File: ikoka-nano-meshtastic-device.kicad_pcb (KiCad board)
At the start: 2 copper layers, 28 x 40 mm, 7 parts, among them J1 Battery, J2 Solar, J3 Qwiic_RA, Q1 Q_PMOS_GSD, U1 Seeed Studio XIAO nRF52840, U2 E22-900M30S

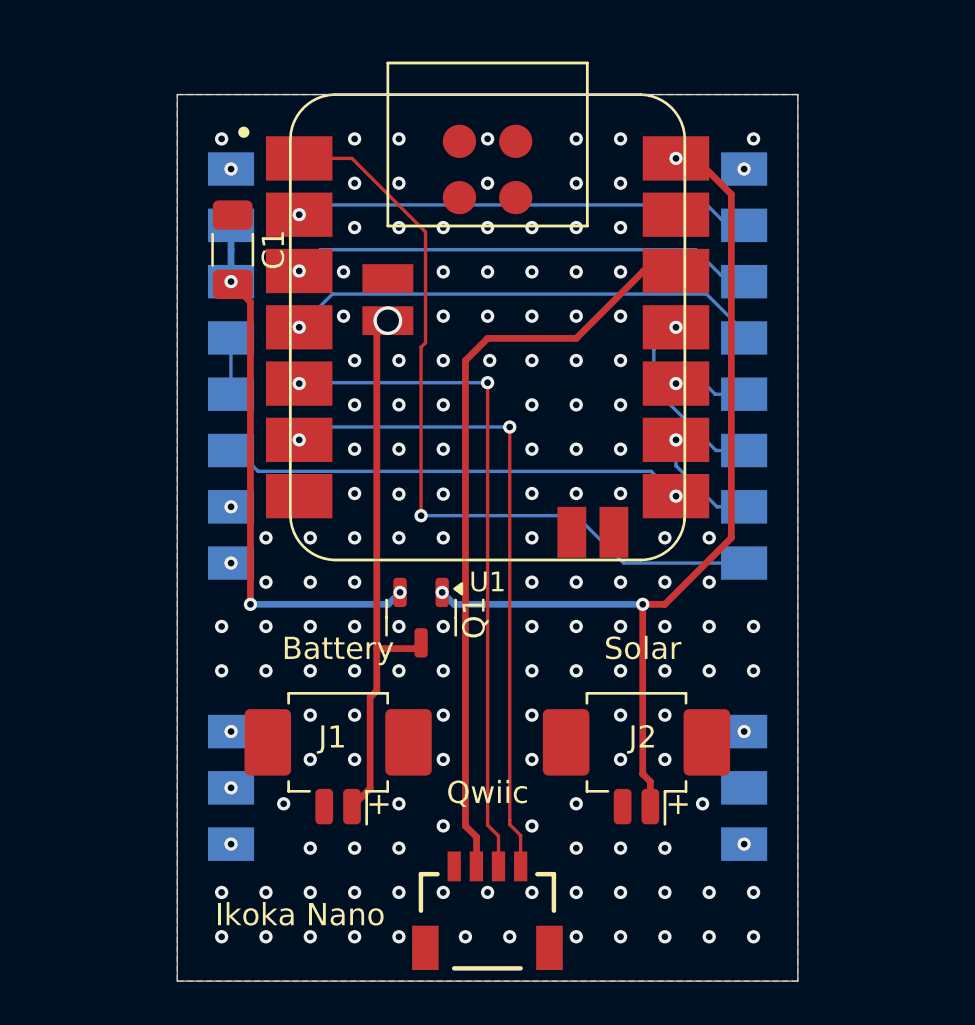
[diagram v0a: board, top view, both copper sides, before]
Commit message: Add missing D1 footprint and update PCB; add LCSC part numbers; remove gerbers
Signed-off-by: Andrew Yong <me@ndoo.sg>
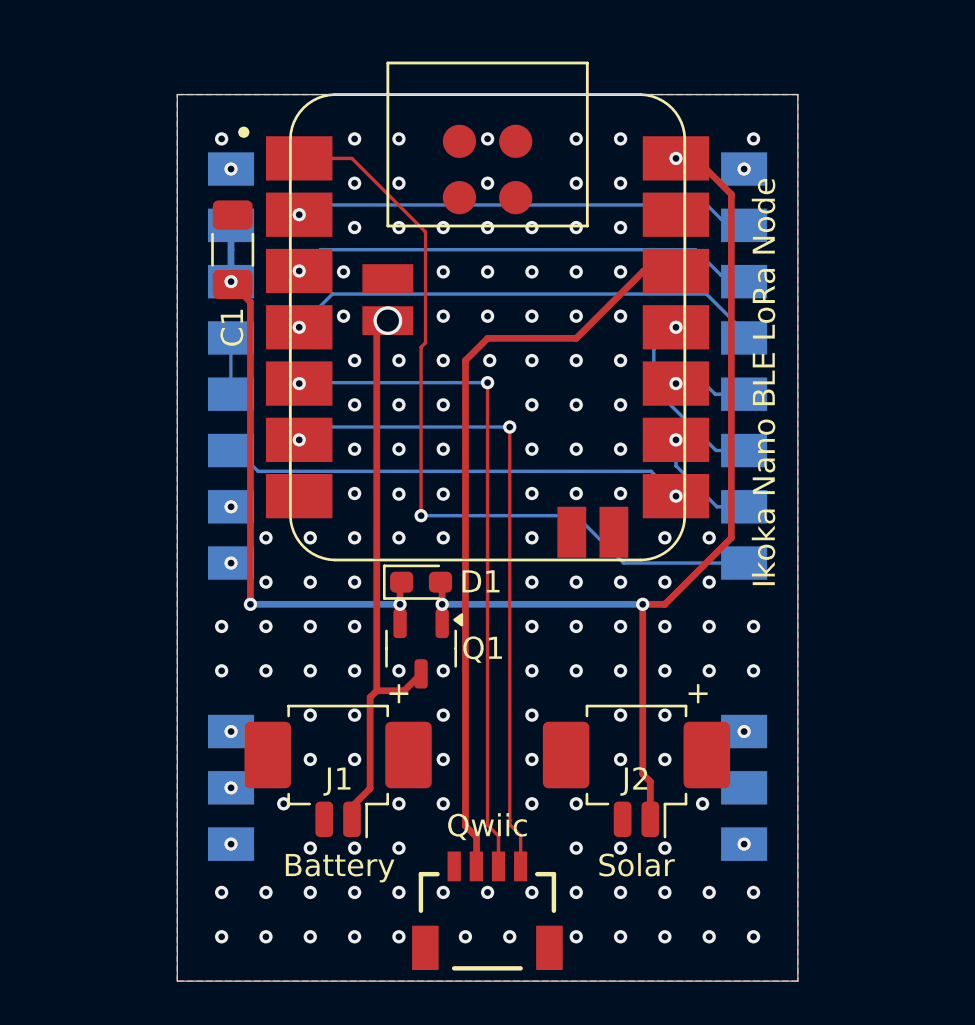
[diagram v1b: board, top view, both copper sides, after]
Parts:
- added D1: NSR20F40NXT5G, Diode_SMD:D_0603_1608Metric_Pad1.05x0.95mm_HandSolder, F.Cu at (147.0, 102.0)
- Q1: value Q_PMOS_GSD -> FDN302P
- moved Q1 1.40 mm to (147.0, 105.0)
- moved J1 0.57 mm to (143.3, 110.3)
- moved J2 0.57 mm to (156.7, 110.3)
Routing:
- net VCC_E22: track 24.9 -> 26.3 mm
- net VBUS: track 43.5 -> 45.0 mm
- net GND: vias 154 -> 152
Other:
- board text added: "Ikoka Nano BLE LoRa Node"
- board text removed: "Ikoka Nano"

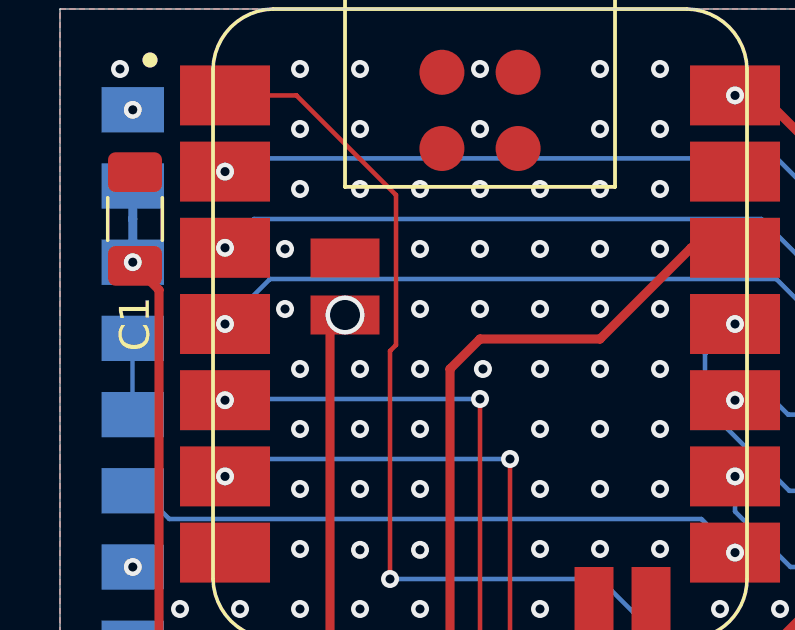
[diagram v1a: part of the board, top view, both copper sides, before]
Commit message: Increase VBAT via size and add teardrop
Signed-off-by: Andrew Yong <me@ndoo.sg>
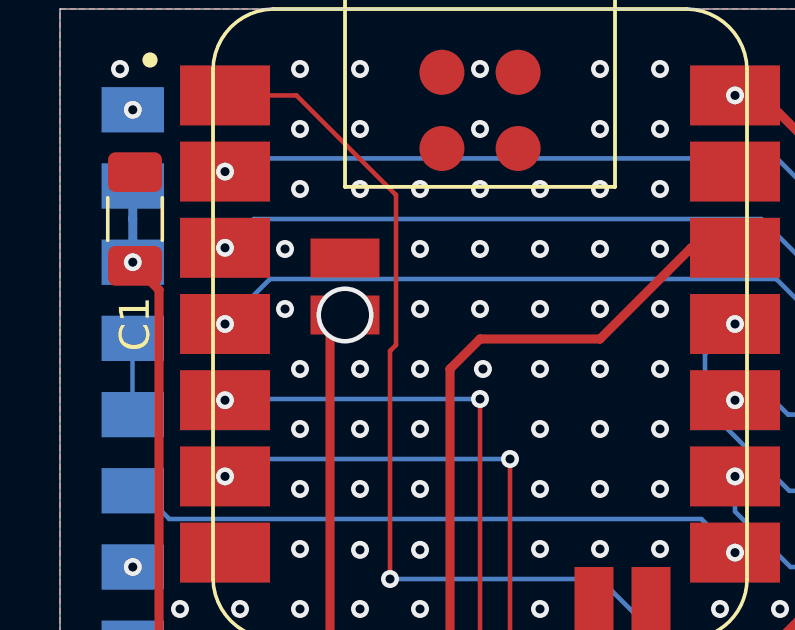
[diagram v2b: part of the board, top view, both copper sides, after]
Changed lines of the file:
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@@
-	)
-	(segment
-		(start 145.026 90.2)
-		(end 144.912 90.314)
-		(width 0.3048)
-		(layer "F.Cu")
-		(net 25)
 	)
 	(segment
@@
 	(via
 		(at 145.5 90.2)
-		(size 1.3)
-		(drill 1)
-		(layers "F.Cu" "B.Cu")
+		(size 1.9)
+		(drill 1.6)
+		(layers "F.Cu" "B.Cu")
+		(teardrops
+			(best_length_ratio 0.5)
+			(max_length 1)
+			(best_width_ratio 1)
+			(max_width 2)
+			(curve_points 10)
+			(filter_ratio 0.9)
+			(enabled yes)
+			(allow_two_segments yes)
+			(prefer_zone_connections yes)
+		)
 		(net 25)
 	)
@@
 	)
 	(zone
+		(net 25)
+		(net_name "VBAT")
+		(layer "F.Cu")
+		(name "$teardrop_padvia$")
+		(hatch full 0.1)
+		(priority 30000)
+		(attr
+			(teardrop
+				(type padvia)
+			)
+		)
+		(connect_pads yes
+			(clearance 0)
+		)
+		(min_thickness 0.0254)
+		(filled_areas_thickness no)
+		(fill yes
+			(thermal_gap 0.5)
+			(thermal_bridge_width 0.5)
+			(island_removal_mode 1)
+			(island_area_min 10)
+		)
+		(polygon
+			(pts
+				(xy 145.1524 91.936512) (xy 145.16687 91.741673) (xy 145.208381 91.592791) (xy 145.274082 91.479995)
+				(xy 145.361119 91.393414) (xy 145.466643 91.32318) (xy 145.587801 91.259422) (xy 145.721743 91.19227)
+				(xy 145.865616 91.111854) (xy 146.016569 91.008304) (xy 146.171751 90.871751) (xy 145.5 90.199)
+				(xy 144.55 90.2) (xy 144.558332 90.438899) (xy 144.58095 90.6343) (xy 144.614281 90.797076) (xy 144.654755 90.938103)
+				(xy 144.6988 91.068256) (xy 144.742844 91.198408) (xy 144.783318 91.339435) (xy 144.816649 91.502211)
+				(xy 144.839267 91.697612) (xy 144.8476 91.936512)
+			)
+		)
+	)
+	(zone

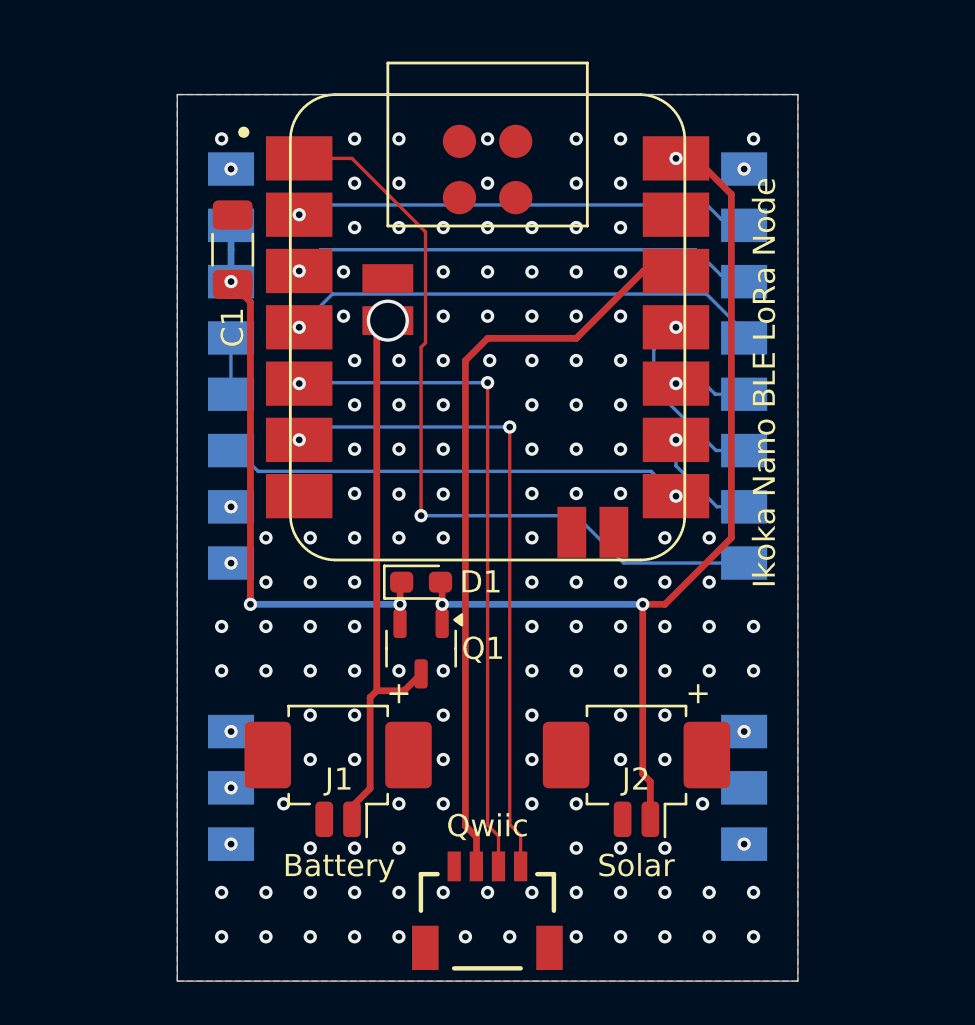
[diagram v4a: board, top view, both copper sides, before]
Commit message: Update Seeed XIAO nRF52840 with BAT+ PTH pad
Signed-off-by: Andrew Yong <me@ndoo.sg>
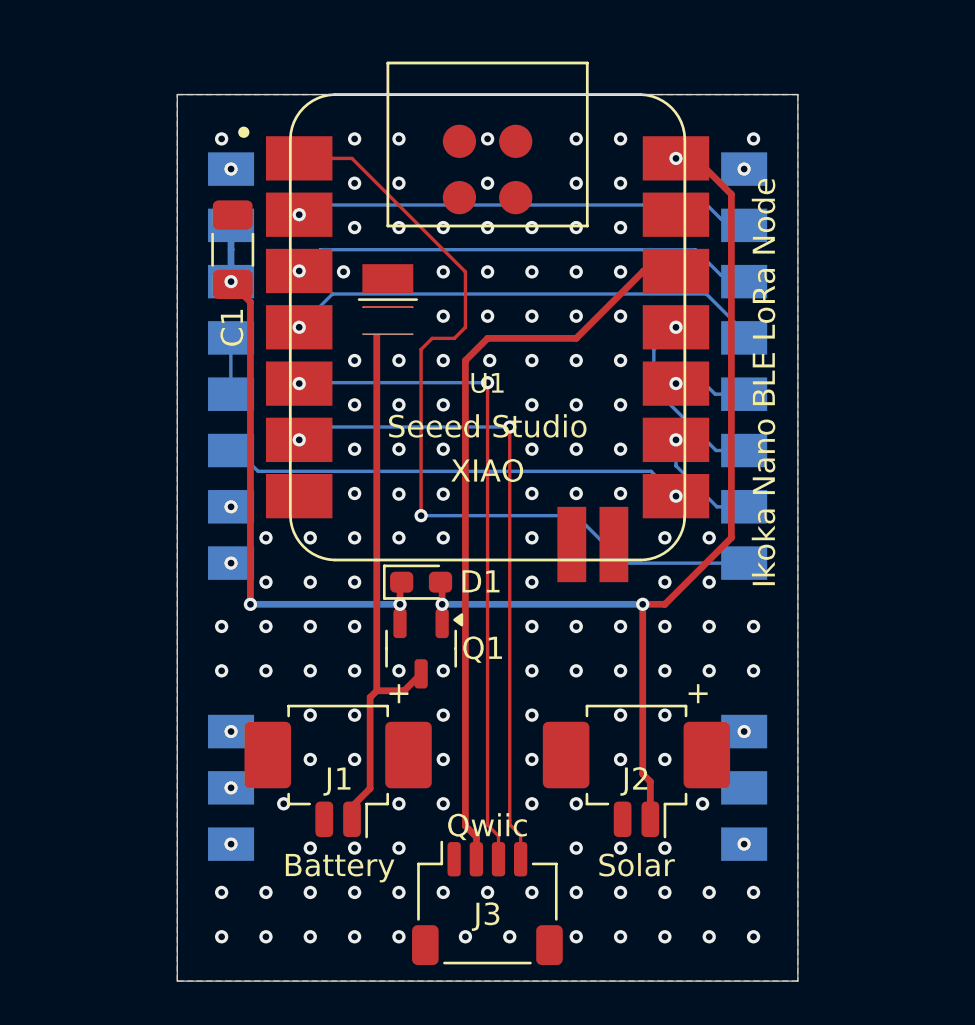
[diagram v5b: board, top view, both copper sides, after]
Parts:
- J3: footprint SparkFun-Connector:JST_SMD_1.0mm-4_RA -> Connector_JST:JST_SH_SM04B-SRSS-TB_1x04-1MP_P1.00mm_Horizontal
- U1: footprint Seeed Studio XIAO Series Library:XIAO-nRF52840-Sense-14P-2.54-21X17.8MM -> Seeed Studio XIAO Series Library:XIAO-nRF52840-BatteryPTH-14P-2.54-21X17.8MM
- moved J3 1.67 mm to (150.0, 116.5)
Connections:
- J3 pad 1: GND -> I2C_SCL
- J3 pad 2: 3V3 -> I2C_SDA
- J3 pad 3: I2C_SDA -> 3V3
- J3 pad 4: I2C_SCL -> GND
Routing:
- net SX126X_CS: track 35.4 -> 37.5 mm
- net VBAT: vias 1 -> 0
- net GND: vias 152 -> 149

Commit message: Switch back to SparkFun Qwiic symbol/footprint, run DRC, fix 3D models
Signed-off-by: Andrew Yong <me@ndoo.sg>
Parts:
- J3: footprint Connector_JST:JST_SH_SM04B-SRSS-TB_1x04-1MP_P1.00mm_Horizontal -> SparkFun-Connector:JST_SMD_1.0mm-4_RA
- moved J3 2.00 mm to (150.0, 114.5)
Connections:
- J3 pad 1: I2C_SCL -> GND
- J3 pad 2: I2C_SDA -> 3V3
- J3 pad 3: 3V3 -> I2C_SDA
- J3 pad 4: GND -> I2C_SCL

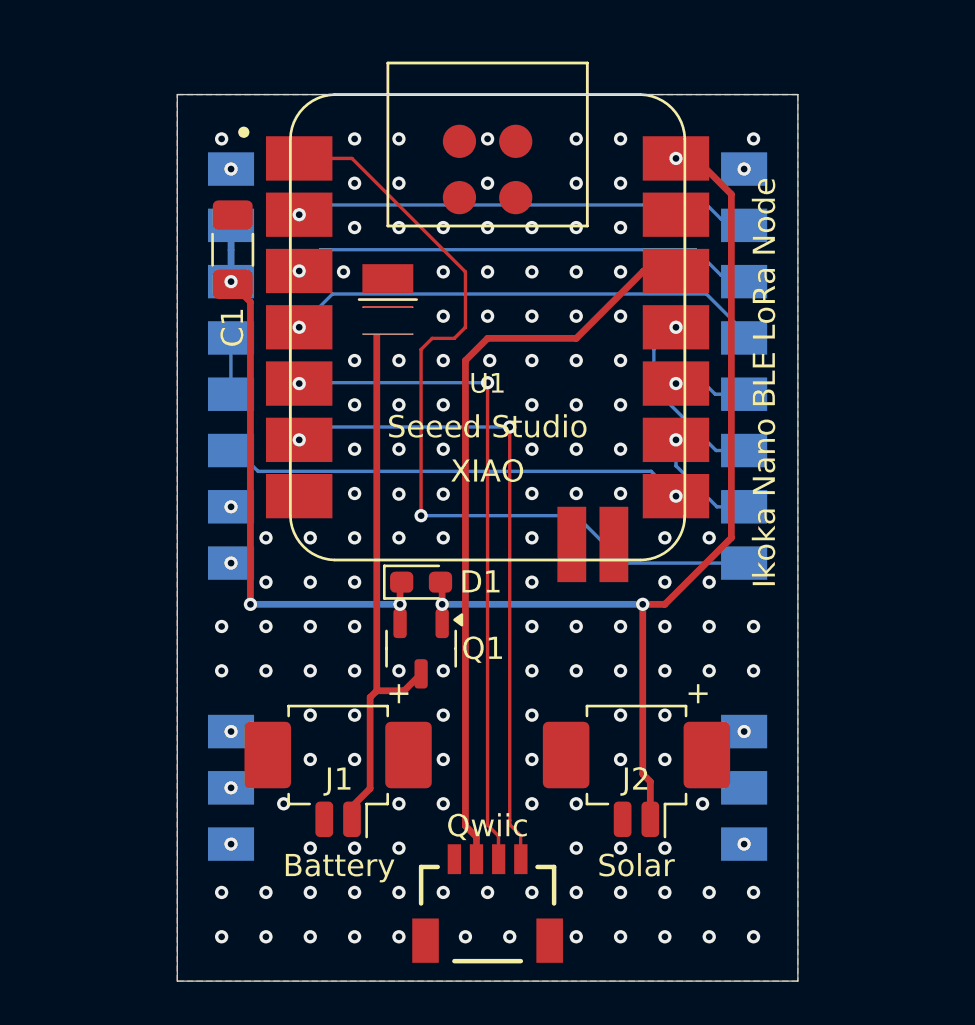
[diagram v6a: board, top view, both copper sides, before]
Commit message: Rebase XIAO BLE hand soldering symbol/footprint on upstream
Signed-off-by: Andrew Yong <me@ndoo.sg>
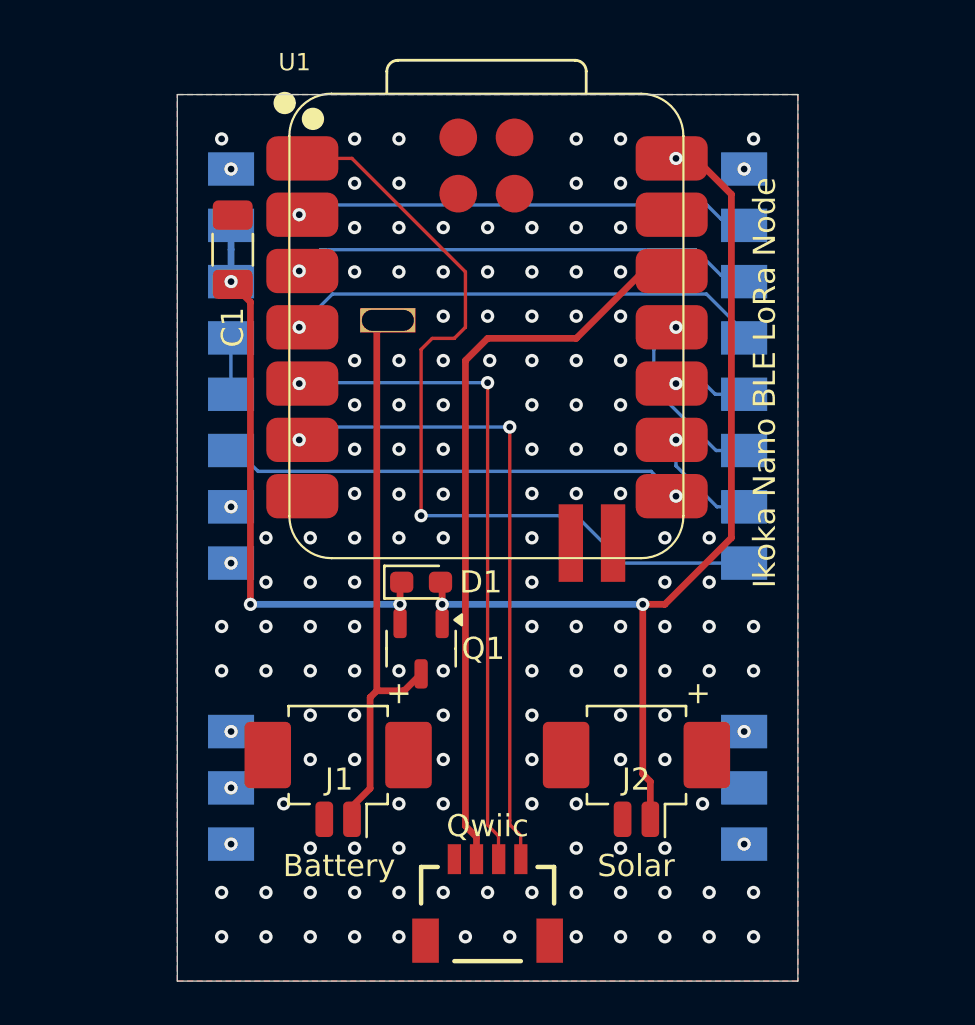
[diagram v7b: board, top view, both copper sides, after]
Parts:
- U1: footprint Seeed Studio XIAO Series Library:XIAO-nRF52840-BatteryPTH-14P-2.54-21X17.8MM -> Seeed Studio XIAO Series Library:XIAO-nRF52840-SMD_Handsoldering
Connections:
- U1 pad 15: unconnected-(U1-PA30_SWCLK-Pad15) -> VBAT
- U1 pad 22: VBAT -> unconnected-(U1-GND-Pad22)
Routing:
- net VBUS: track 45.0 -> 44.1 mm
- net GND: vias 149 -> 148

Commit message: Add 5.4V boost converter circuit, use more JLCPCB basic parts, make PCB square, add internal battery connector
Signed-off-by: Andrew Yong <me@ndoo.sg>
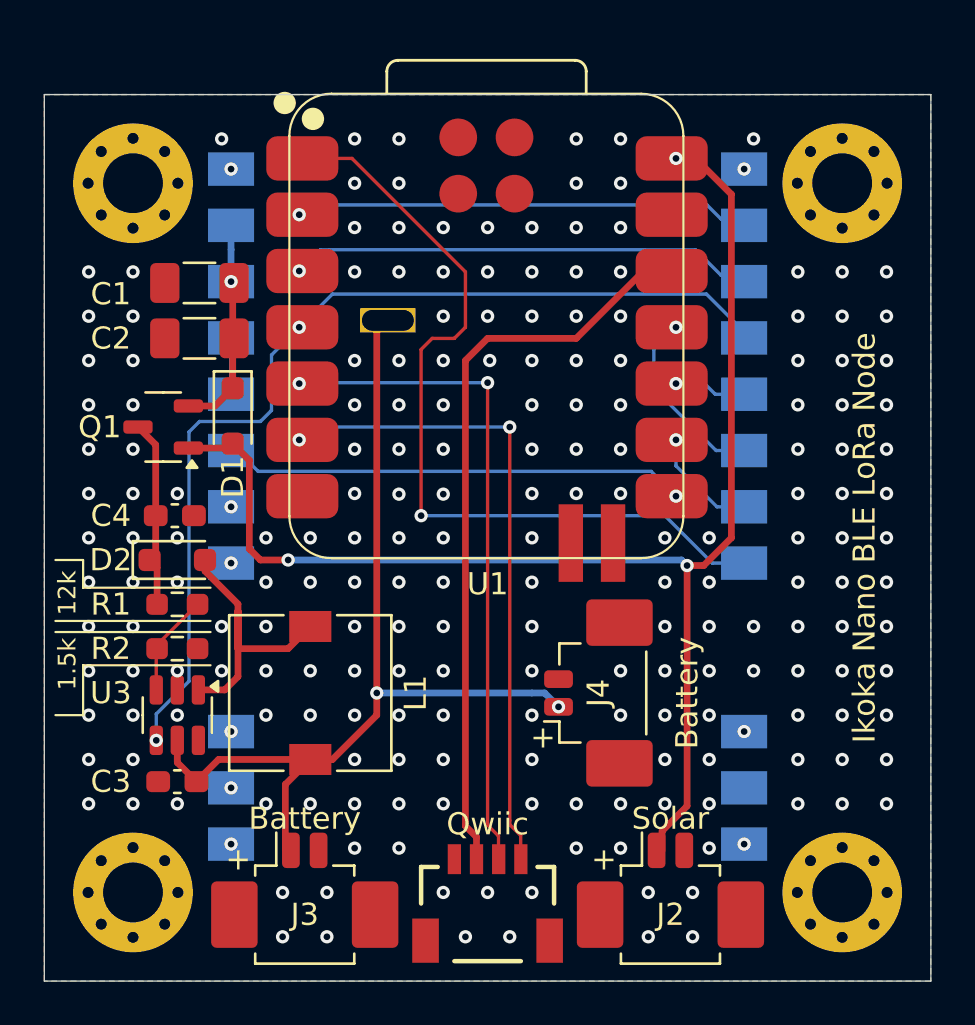
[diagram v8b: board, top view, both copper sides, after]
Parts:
- added C2: 100uF, Capacitor_SMD:C_1206_3216Metric_Pad1.33x1.80mm_HandSolder, F.Cu at (137.0, 91.0)
- added C3: 22uF, Capacitor_SMD:C_0603_1608Metric_Pad1.08x0.95mm_HandSolder, F.Cu at (136.0, 111.0)
- added C4: 22uF, Capacitor_SMD:C_0603_1608Metric_Pad1.08x0.95mm_HandSolder, F.Cu at (135.9, 99.0)
- added D2: D_Schottky, Diode_SMD:D_SOD-323_HandSoldering, F.Cu at (136.0, 101.0)
- added H1: MountingHole_Pad, MountingHole:MountingHole_2.7mm_M2.5_Pad_Via, F.Cu at (134.0, 84.0)
- added H2: MountingHole_Pad, MountingHole:MountingHole_2.7mm_M2.5_Pad_Via, F.Cu at (166.0, 84.0)
- added H3: MountingHole_Pad, MountingHole:MountingHole_2.7mm_M2.5_Pad_Via, F.Cu at (134.0, 116.0)
- added H4: MountingHole_Pad, MountingHole:MountingHole_2.7mm_M2.5_Pad_Via, F.Cu at (166.0, 116.0)
- added J4: Battery, Connector_Molex:Molex_PicoBlade_53398-0271_1x02-1MP_P1.25mm_Vertical, F.Cu at (154.4, 107.0)
- added L1: 22uH, Inductor_SMD:L_SXN_SMDRI64, F.Cu at (142.0, 107.0)
- added R1: 12k, Resistor_SMD:R_0603_1608Metric_Pad0.98x0.95mm_HandSolder, F.Cu at (136.0, 103.0)
- added R2: 1.5k, Resistor_SMD:R_0603_1608Metric_Pad0.98x0.95mm_HandSolder, F.Cu at (136.0, 105.0)
- added U3: MT3608, Package_TO_SOT_SMD:SOT-23-6, F.Cu at (136.0, 108.0)
- D1: value NSR20F40NXT5G -> D_Schottky; footprint Diode_SMD:D_0603_1608Metric_Pad1.05x0.95mm_HandSolder -> Diode_SMD:D_SOD-323_HandSoldering
- moved Q1 15.3 mm to (135.4, 95.0), turned to 180 degrees
- moved D1 11.3 mm to (138.5, 94.5), turned to -90 degrees
- moved J2 6.39 mm to (158.2, 116.5), turned to 0 degrees
- moved J3 6.38 mm to (141.8, 116.5), turned to 0 degrees
- moved C1 2.12 mm to (137.0, 88.5), turned to 0 degrees
- renumbered J3 to J1, J1 to J3
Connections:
- Q1 pad 3: VBAT -> 5V
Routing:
- net SX126X_RESET: track 21.4 -> 44.3 mm, vias 1 -> 2
- net VBAT: track 24.9 -> 42.6 mm, vias 0 -> 2
- net VBUS: track 44.1 -> 61.7 mm
- net VCC_E22: track 26.3 -> 10.3 mm, vias 3 -> 1
- net SW: track 0.00 -> 15.0 mm
- net 5V: track 0.00 -> 8.59 mm
- net Net-(U3-FB): track 0.00 -> 4.85 mm
- net GND: track 0.00 -> 0.03 mm, vias 148 -> 213
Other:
- board size 28 x 40 mm -> 40 x 40 mm
- board text added: "JLCJLCJLCJLC"
